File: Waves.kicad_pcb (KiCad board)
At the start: 4 copper layers, 49.8 x 106.5 mm, 151 parts, among them J1 AudioJack2_SwitchT, J10 AudioJack2_SwitchT, J11 Conn_01x04_Male, J12 Conn_01x04_Male, J13 AudioJack2_SwitchT, J14 AudioJack2_SwitchT, J15 Conn_02x05_Odd_Even, J2 AudioJack2_SwitchT, J3 AudioJack2_SwitchT, J4 AudioJack2_SwitchT, J5 AudioJack2_SwitchT, J6 AudioJack2_SwitchT, J7 AudioJack2_SwitchT, J8 AudioJack2_SwitchT, J9 AudioJack2_SwitchT, Q1 BC847, Q2 BC847, Q3 BC847, Q4 BC847, Q5 BC847, Q6 BC847, SW1 SW_Push, SW2 Rotary_Encoder_Switch, SW3 SW_Push_LED, SW4 SW_Push_LED, SW5 SW_Push_LED, SW6 SW_Push_LED, U1 STM32G431, U2 AT25xxx, U3 IPS240x240, U4 PCM5100, U5 TL072, U6 R-78E3.3-0.5, U7 LD2981ABU33TR, U8 MCP6004, U9 MCP6004, Y1 8MHz

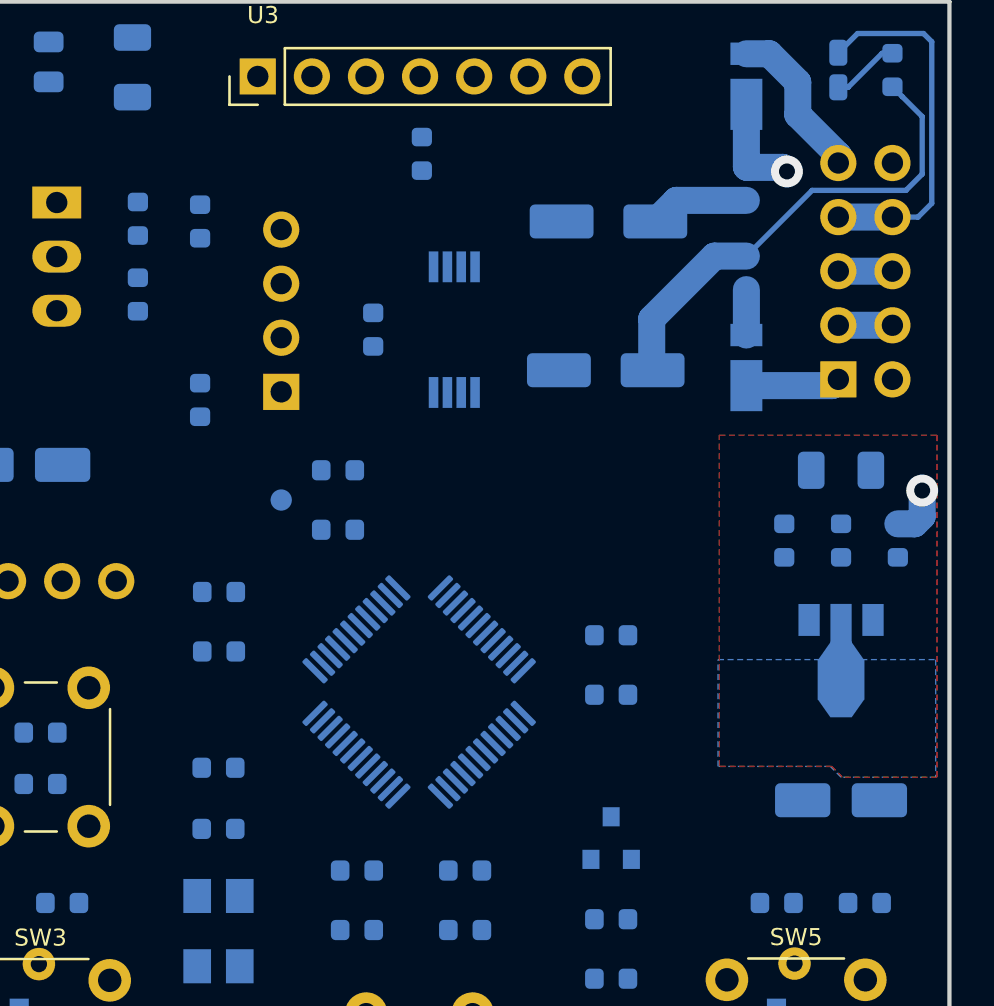
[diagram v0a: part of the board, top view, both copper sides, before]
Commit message: Via stitch on headsink.
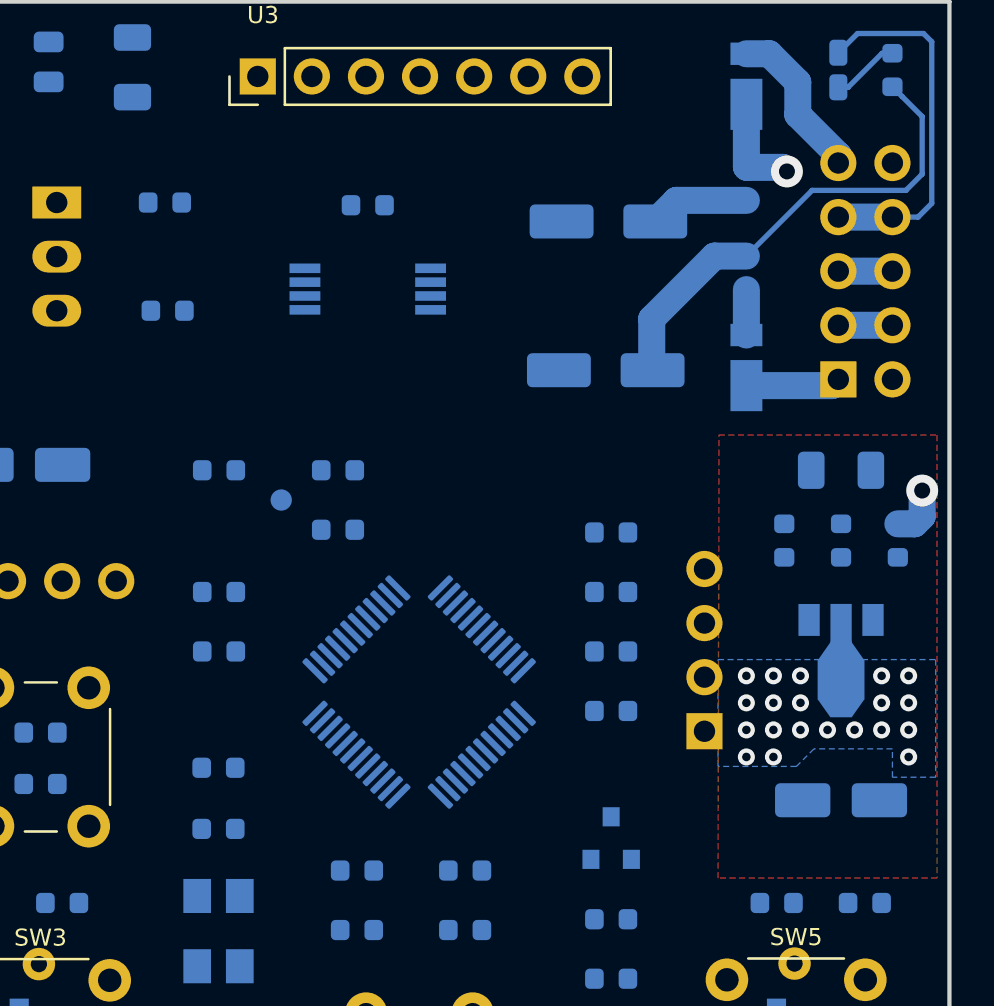
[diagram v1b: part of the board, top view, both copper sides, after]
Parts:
- moved J12 25.5 mm to (140.3, 82.6)
- moved R3 24.2 mm to (135.9, 73.3), turned to 0 degrees
- moved R4 24.2 mm to (135.9, 81.7), turned to 0 degrees
- moved R9 17.6 mm to (117.5, 70.4), turned to 0 degrees
- moved C14 5.85 mm to (124.5, 57.9), turned to 0 degrees
- moved U2 4.49 mm to (124.5, 61.8), turned to 180 degrees
- moved C9 2.03 mm to (135.9, 76.1)
- moved C11 2.03 mm to (135.9, 78.9)
- moved C38 1.59 mm to (115.1, 62.9), turned to 0 degrees
- moved C36 1.48 mm to (114.9, 57.8), turned to 0 degrees
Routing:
- net GND: vias 0 -> 20

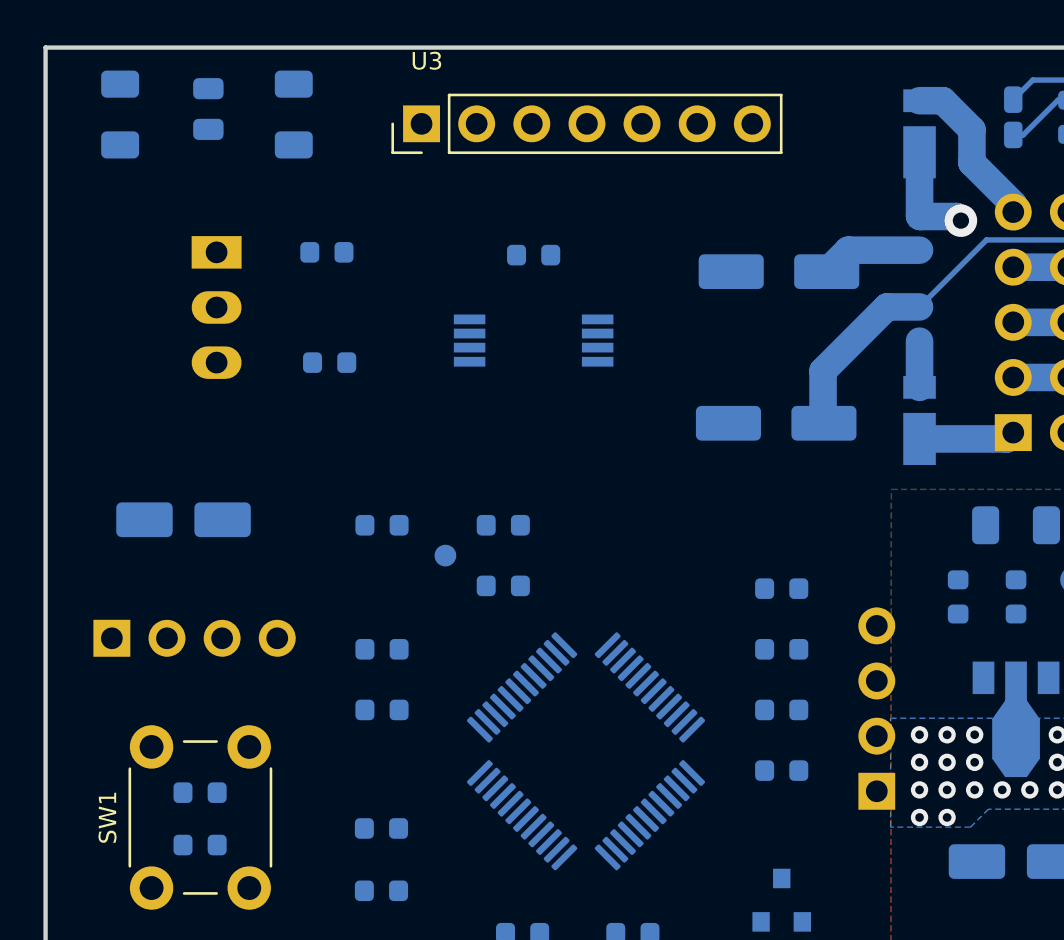
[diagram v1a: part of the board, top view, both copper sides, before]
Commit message: Swap IC2 and SWD headers.
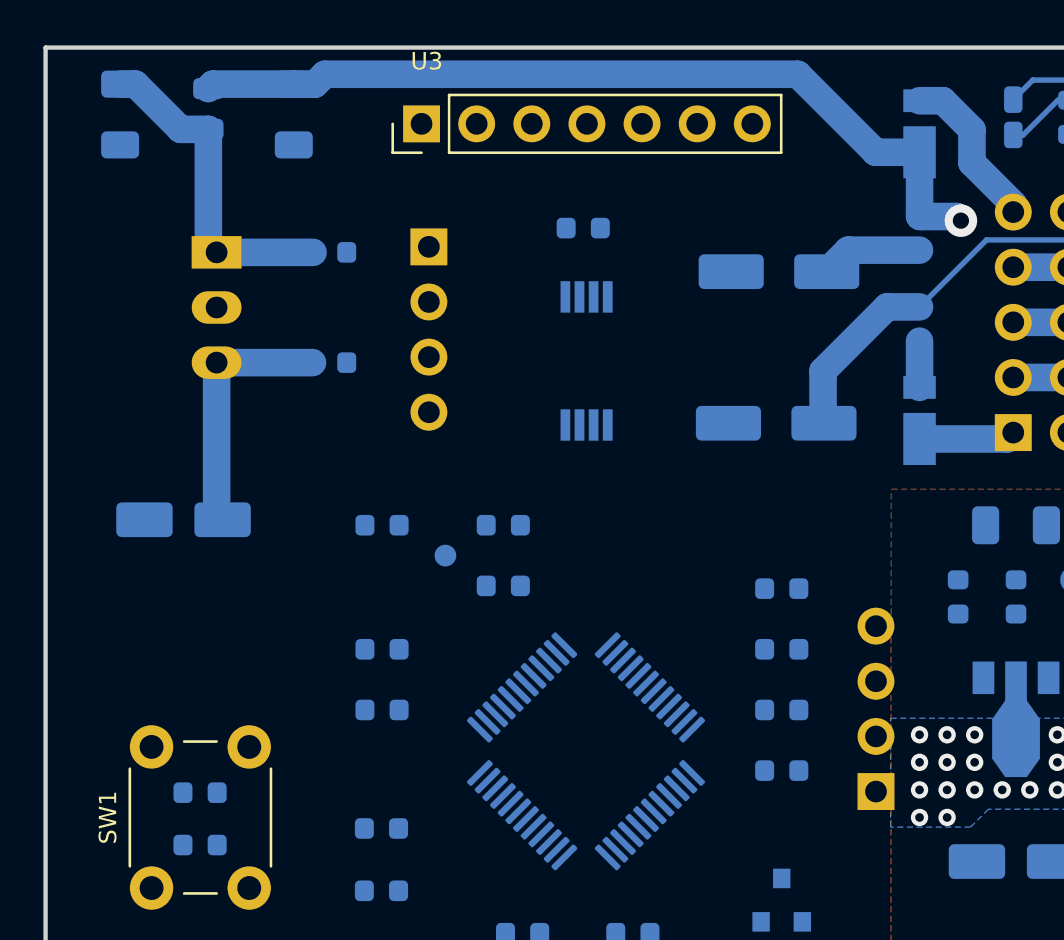
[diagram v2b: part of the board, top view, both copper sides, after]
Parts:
- moved J11 35.9 mm to (140.2, 82.6), turned to 0 degrees
- moved J12 32.5 mm to (119.6, 57.5), turned to 180 degrees
- moved U2 2.61 mm to (126.9, 62.8), turned to 90 degrees
- moved C14 2.60 mm to (126.7, 56.7), turned to 180 degrees
- moved C36 0.13 mm to (115.1, 57.8)
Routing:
- net Net-(C31-Pad1): track 26.2 -> 60.7 mm
- net Net-(C34-Pad1): track 0.00 -> 15.2 mm
- net +3V3: track 0.00 -> 11.8 mm
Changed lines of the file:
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@@
     (thickness 1.6)
     (drawings 75)
-    (tracks 67)
+    (tracks 83)
     (zones 0)
     (modules 151)
@@
   )
   (setup
-    (last_trace_width 0.25)
+    (last_trace_width 1.27)
     (user_trace_width 0.635)
     (user_trace_width 1.27)
@@
   )
   (module Package_SO:TSSOP-8_4.4x3mm_P0.65mm placed (layer B.Cu)
-    (at 124.46 61.849 180)
+    (at 126.8984 62.7888 90)
     (descr "8-Lead Plastic Thin Shrink Small Outline (ST)-4.4 mm Body [TSSOP] (see Microchip Packaging Specification 00000049BS.pdf)")
     (tags "SSOP 0.65")
     (attr smd)
-    (fp_text reference U2 (at 0 2.55) (layer B.SilkS)
+    (fp_text reference U2 (at 0 2.55 90) (layer B.SilkS)
       (effects (font (size 0.8 0.8) (thickness 0.12)) (justify mirror))
     )
-    (fp_text value AT25xxx (at 0 -2.55) (layer B.Fab)
+    (fp_text value AT25xxx (at 0 -2.55 90) (layer B.Fab)
       (effects (font (size 0.8 0.8) (thickness 0.12)) (justify mirror))
     )
-    (fp_text user %R (at 0 0) (layer B.Fab)
+    (fp_text user %R (at 0 0 90) (layer B.Fab)
       (effects (font (size 0.8 0.8) (thickness 0.12)) (justify mirror))
     )
@@
     (fp_line (start 2.2 1.5) (end 2.2 -1.5) (layer B.Fab) (width 0.15))
     (fp_line (start -1.2 1.5) (end 2.2 1.5) (layer B.Fab) (width 0.15))
-    (pad 8 smd rect (at 2.95 0.975 180) (size 1.45 0.45) (layers B.Cu B.Paste B.Mask)
+    (pad 8 smd rect (at 2.95 0.975 90) (size 1.45 0.45) (layers B.Cu B.Paste B.Mask)
       (net 76 +3V3))
-    (pad 7 smd rect (at 2.95 0.325 180) (size 1.45 0.45) (layers B.Cu B.Paste B.Mask)
+    (pad 7 smd rect (at 2.95 0.325 90) (size 1.45 0.45) (layers B.Cu B.Paste B.Mask)
       (net 76 +3V3))
-    (pad 6 smd rect (at 2.95 -0.325 180) (size 1.45 0.45) (layers B.Cu B.Paste B.Mask)
+    (pad 6 smd rect (at 2.95 -0.325 90) (size 1.45 0.45) (layers B.Cu B.Paste B.Mask)
       (net 70 MEM_SCK))
-    (pad 5 smd rect (at 2.95 -0.975 180) (size 1.45 0.45) (layers B.Cu B.Paste B.Mask)
+    (pad 5 smd rect (at 2.95 -0.975 90) (size 1.45 0.45) (layers B.Cu B.Paste B.Mask)
       (net 68 MEM_MOSI))
-    (pad 4 smd rect (at -2.95 -0.975 180) (size 1.45 0.45) (layers B.Cu B.Paste B.Mask)
+    (pad 4 smd rect (at -2.95 -0.975 90) (size 1.45 0.45) (layers B.Cu B.Paste B.Mask)
       (net 75 GND))
-    (pad 3 smd rect (at -2.95 -0.325 180) (size 1.45 0.45) (layers B.Cu B.Paste B.Mask)
+    (pad 3 smd rect (at -2.95 -0.325 90) (size 1.45 0.45) (layers B.Cu B.Paste B.Mask)
       (net 76 +3V3))
-    (pad 2 smd rect (at -2.95 0.325 180) (size 1.45 0.45) (layers B.Cu B.Paste B.Mask)
+    (pad 2 smd rect (at -2.95 0.325 90) (size 1.45 0.45) (layers B.Cu B.Paste B.Mask)
       (net 69 MEM_MISO))
-    (pad 1 smd rect (at -2.95 0.975 180) (size 1.45 0.45) (layers B.Cu B.Paste B.Mask)
+    (pad 1 smd rect (at -2.95 0.975 90) (size 1.45 0.45) (layers B.Cu B.Paste B.Mask)
       (net 71 MEM_CS))
     (model ${KISYS3DMOD}/Package_SO.3dshapes/TSSOP-8_4.4x3mm_P0.65mm.wrl
@@
   )
   (module Connector_PinHeader_2.54mm:PinHeader_1x04_P2.54mm_Vertical placed (layer B.Cu)
-    (at 140.2715 82.6135)
+    (at 119.634 57.531 180)
     (descr "Through hole straight pin header, 1x04, 2.54mm pitch, single row")
     (tags "Through hole pin header THT 1x04 2.54mm single row")
@@
     (fp_line (start 1.27 1.27) (end 1.27 -8.89) (layer B.Fab) (width 0.1))
     (fp_line (start -0.635 1.27) (end 1.27 1.27) (layer B.Fab) (width 0.1))
-    (pad 4 thru_hole oval (at 0 -7.62) (size 1.7 1.7) (drill 1) (layers *.Cu *.Mask)
+    (pad 4 thru_hole oval (at 0 -7.62 180) (size 1.7 1.7) (drill 1) (layers *.Cu *.Mask)
       (net 40 I2C_SDA))
-    (pad 3 thru_hole oval (at 0 -5.08) (size 1.7 1.7) (drill 1) (layers *.Cu *.Mask)
+    (pad 3 thru_hole oval (at 0 -5.08 180) (size 1.7 1.7) (drill 1) (layers *.Cu *.Mask)
       (net 75 GND))
-    (pad 2 thru_hole oval (at 0 -2.54) (size 1.7 1.7) (drill 1) (layers *.Cu *.Mask)
+    (pad 2 thru_hole oval (at 0 -2.54 180) (size 1.7 1.7) (drill 1) (layers *.Cu *.Mask)
       (net 41 I2C_SCL))
-    (pad 1 thru_hole rect (at 0 0) (size 1.7 1.7) (drill 1) (layers *.Cu *.Mask)
+    (pad 1 thru_hole rect (at 0 0 180) (size 1.7 1.7) (drill 1) (layers *.Cu *.Mask)
       (net 75 GND))
     (model ${KISYS3DMOD}/Connector_PinHeader_2.54mm.3dshapes/PinHeader_1x04_P2.54mm_Vertical.wrl
@@
   )
   (module Connector_PinHeader_2.54mm:PinHeader_1x04_P2.54mm_Vertical placed (layer B.Cu)
-    (at 105.029 75.565 270)
+    (at 140.2334 82.6262)
     (descr "Through hole straight pin header, 1x04, 2.54mm pitch, single row")
     (tags "Through hole pin header THT 1x04 2.54mm single row")
-    (fp_text reference J11 (at 0 2.33 90) (layer B.SilkS)
+    (fp_text reference J11 (at 0 2.33) (layer B.SilkS)
       (effects (font (size 0.8 0.8) (thickness 0.12)) (justify mirror))
     )
-    (fp_text value Conn_01x04_Male (at 0 -9.95 90) (layer B.Fab)
+    (fp_text value Conn_01x04_Male (at 0 -9.95) (layer B.Fab)
       (effects (font (size 0.8 0.8) (thickness 0.12)) (justify mirror))
     )
-    (fp_text user %R (at 0 -3.81 180) (layer B.Fab)
+    (fp_text user %R (at 0 -3.81 -90) (layer B.Fab)
       (effects (font (size 0.8 0.8) (thickness 0.12)) (justify mirror))
     )
@@
     (fp_line (start 1.27 1.27) (end 1.27 -8.89) (layer B.Fab) (width 0.1))
     (fp_line (start -0.635 1.27) (end 1.27 1.27) (layer B.Fab) (width 0.1))
-    (pad 4 thru_hole oval (at 0 -7.62 270) (size 1.7 1.7) (drill 1) (layers *.Cu *.Mask)
+    (pad 4 thru_hole oval (at 0 -7.62) (size 1.7 1.7) (drill 1) (layers *.Cu *.Mask)
       (net 2 RESET))
-    (pad 3 thru_hole oval (at 0 -5.08 270) (size 1.7 1.7) (drill 1) (layers *.Cu *.Mask)
+    (pad 3 thru_hole oval (at 0 -5.08) (size 1.7 1.7) (drill 1) (layers *.Cu *.Mask)
       (net 38 SWDIO))
-    (pad 2 thru_hole oval (at 0 -2.54 270) (size 1.7 1.7) (drill 1) (layers *.Cu *.Mask)
+    (pad 2 thru_hole oval (at 0 -2.54) (size 1.7 1.7) (drill 1) (layers *.Cu *.Mask)
       (net 39 SWCLK))
-    (pad 1 thru_hole rect (at 0 0 270) (size 1.7 1.7) (drill 1) (layers *.Cu *.Mask)
+    (pad 1 thru_hole rect (at 0 0) (size 1.7 1.7) (drill 1) (layers *.Cu *.Mask)
       (net 75 GND))
     (model ${KISYS3DMOD}/Connector_PinHeader_2.54mm.3dshapes/PinHeader_1x04_P2.54mm_Vertical.wrl
@@
   )
   (module Capacitor_SMD:C_0603_1608Metric placed (layer B.Cu)
-    (at 114.935 57.785)
+    (at 115.062 57.785)
     (descr "Capacitor SMD 0603 (1608 Metric), square (rectangular) end terminal, IPC_7351 nominal, (Body size source: http://www.tortai-tech.com/upload/download/2011102023233369053.pdf), generated with kicad-footprint-generator")
     (tags capacitor)
@@
   )
   (module Capacitor_SMD:C_0603_1608Metric placed (layer B.Cu)
-    (at 124.46 57.912)
+    (at 126.746 56.6674 180)
     (descr "Capacitor SMD 0603 (1608 Metric), square (rectangular) end terminal, IPC_7351 nominal, (Body size source: http://www.tortai-tech.com/upload/download/2011102023233369053.pdf), generated with kicad-footprint-generator")
     (tags capacitor)
@@
     (fp_line (start -0.8 0.4) (end 0.8 0.4) (layer B.Fab) (width 0.1))
     (fp_line (start -0.8 -0.4) (end -0.8 0.4) (layer B.Fab) (width 0.1))
-    (pad 2 smd roundrect (at 0.7875 0) (size 0.875 0.95) (layers B.Cu B.Paste B.Mask) (roundrect_rratio 0.25)
+    (pad 2 smd roundrect (at 0.7875 0 180) (size 0.875 0.95) (layers B.Cu B.Paste B.Mask) (roundrect_rratio 0.25)
       (net 75 GND))
-    (pad 1 smd roundrect (at -0.7875 0) (size 0.875 0.95) (layers B.Cu B.Paste B.Mask) (roundrect_rratio 0.25)
+    (pad 1 smd roundrect (at -0.7875 0 180) (size 0.875 0.95) (layers B.Cu B.Paste B.Mask) (roundrect_rratio 0.25)
       (net 76 +3V3))
     (model ${KISYS3DMOD}/Capacitor_SMD.3dshapes/C_0603_1608Metric.wrl
@@
   (via (at 143.51 83.82) (size 0.8) (drill 0.4) (layers F.Cu B.Cu) (net 75))
   (via (at 142.24 83.82) (size 0.8) (drill 0.4) (layers F.Cu B.Cu) (net 75))
+  (segment (start 109.855 69.828) (end 110.131 70.104) (width 1.27) (layer B.Cu) (net 76))
+  (segment (start 109.855 62.865) (end 109.855 69.828) (width 1.27) (layer B.Cu) (net 76))
+  (segment (start 109.855 62.865) (end 114.2745 62.865) (width 1.27) (layer B.Cu) (net 76))
   (segment (start 142.24 56.1085) (end 142.24 53.174) (width 1.27) (layer B.Cu) (net 88))
   (segment (start 149.352 72.8725) (end 150.1395 72.8725) (width 1.27) (layer B.Cu) (net 88))
@@
   (segment (start 142.24 56.1085) (end 142.2655 56.134) (width 1.27) (layer B.Cu) (net 88))
   (segment (start 142.2655 56.134) (end 143.9545 56.134) (width 1.27) (layer B.Cu) (net 88))
+  (segment (start 114.386 50.035) (end 113.411 50.035) (width 1.27) (layer B.Cu) (net 88))
+  (segment (start 114.8402 49.5808) (end 114.386 50.035) (width 1.27) (layer B.Cu) (net 88))
+  (segment (start 136.6268 49.5808) (end 114.8402 49.5808) (width 1.27) (layer B.Cu) (net 88))
+  (segment (start 142.24 53.174) (end 140.22 53.174) (width 1.27) (layer B.Cu) (net 88))
+  (segment (start 140.22 53.174) (end 136.6268 49.5808) (width 1.27) (layer B.Cu) (net 88))
+  (segment (start 109.6825 50.035) (end 109.474 50.2435) (width 1.27) (layer B.Cu) (net 88))
+  (segment (start 113.411 50.035) (end 109.6825 50.035) (width 1.27) (layer B.Cu) (net 88))
+  (segment (start 109.474 57.404) (end 109.855 57.785) (width 1.27) (layer B.Cu) (net 89))
+  (segment (start 109.474 52.1185) (end 109.474 57.404) (width 1.27) (layer B.Cu) (net 89))
+  (segment (start 108.2017 52.1185) (end 109.474 52.1185) (width 1.27) (layer B.Cu) (net 89))
+  (segment (start 105.41 50.035) (end 106.1182 50.035) (width 1.27) (layer B.Cu) (net 89))
+  (segment (start 106.1182 50.035) (end 108.2017 52.1185) (width 1.27) (layer B.Cu) (net 89))
+  (segment (start 109.855 57.785) (end 114.3 57.785) (width 1.27) (layer B.Cu) (net 89))
   (zone (net 75) (net_name GND) (layer In2.Cu) (hatch edge 0.508)
     (connect_pads (clearance 0.508))
